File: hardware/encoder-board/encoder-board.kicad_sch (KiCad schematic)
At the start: 10 parts, among them J1 Conn_01x04, U1 ITR1204SR10A_TR(BY), U2 ITR1204SR10A_TR(BY)

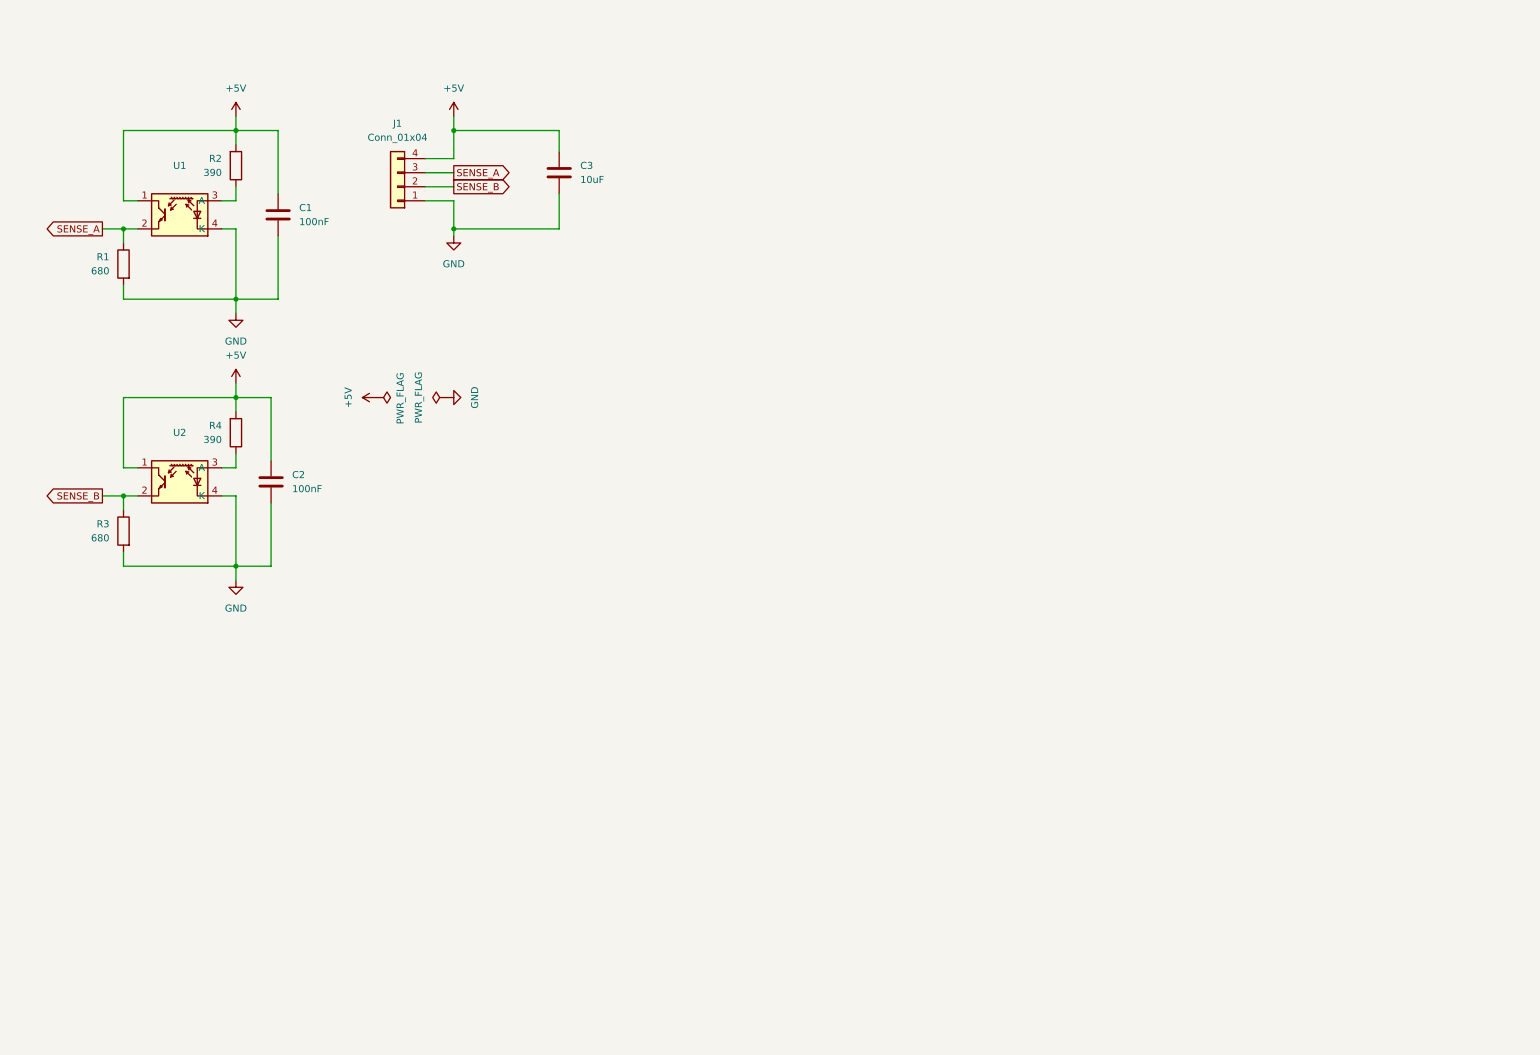
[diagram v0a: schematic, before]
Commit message: fix encoder board references
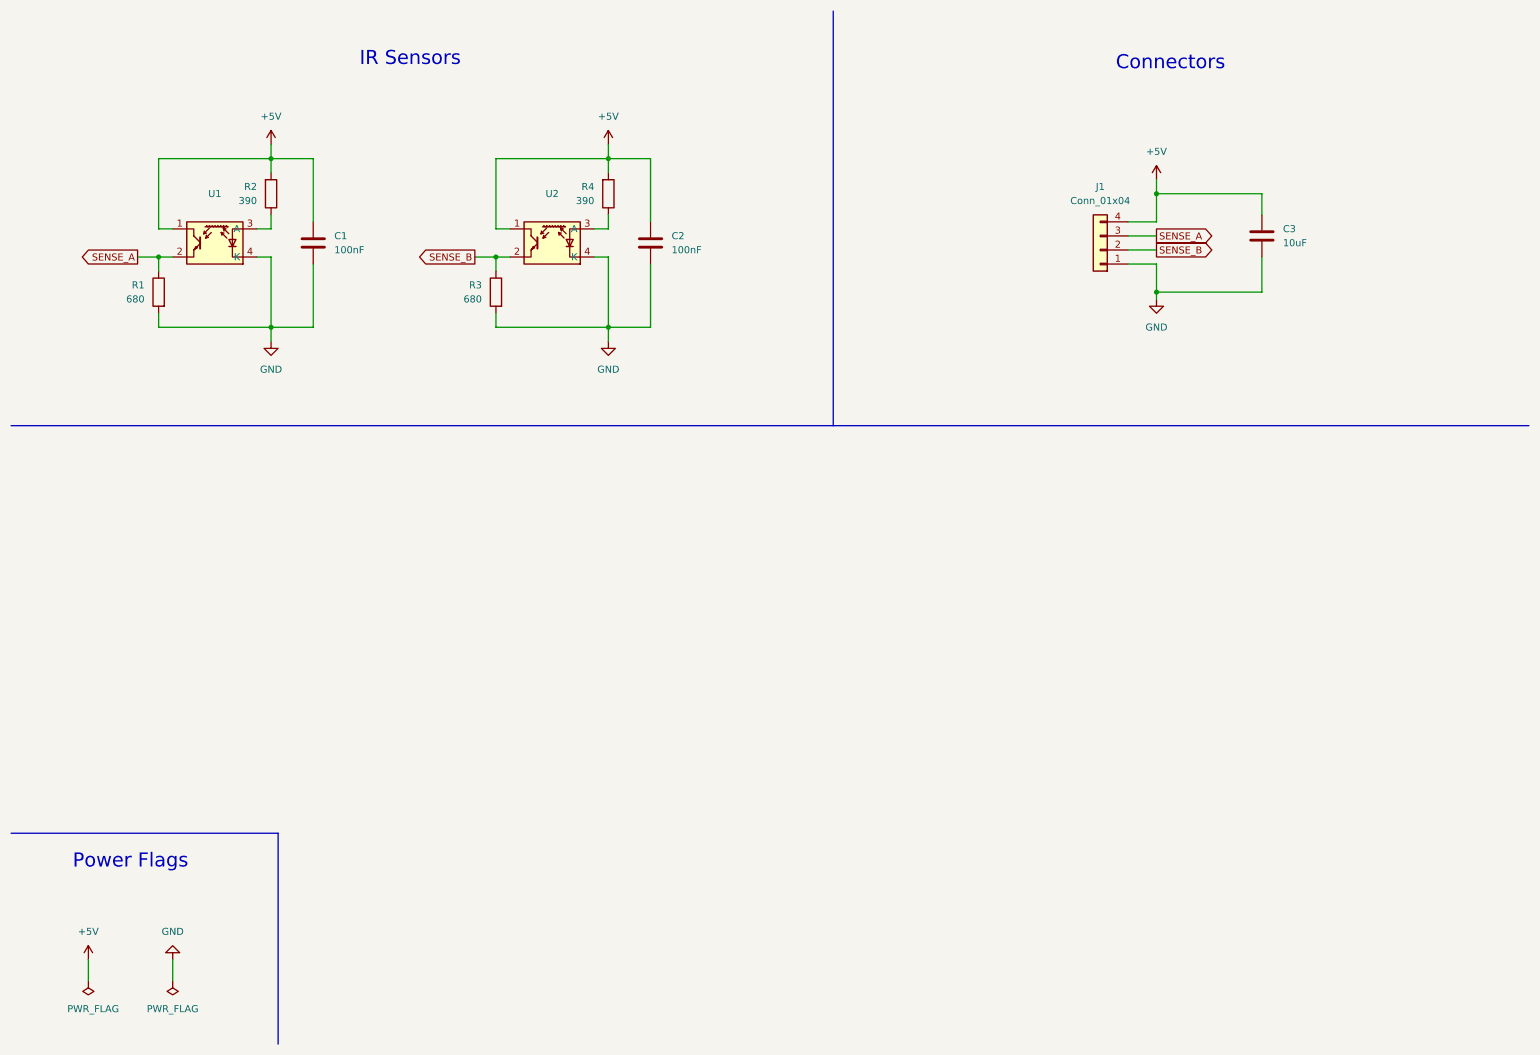
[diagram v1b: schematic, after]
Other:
- note added: "Connectors"
- note added: "IR Sensors"
- note added: "Power Flags"
- moved on the sheet: C1, C2, C3, J1, R1, R2, R3, R4, U1, U2
